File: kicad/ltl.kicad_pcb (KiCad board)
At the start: 2 copper layers, 98.6 x 63.2 mm, 66 parts, among them J1 J1, Q1 RUM001L02T2CL, Q2 RZM001P02T2L, Q3 BC327, U1 TPL5111, U2 ESP-12E, U3 DS18B20, U4 TPS73733DCQR

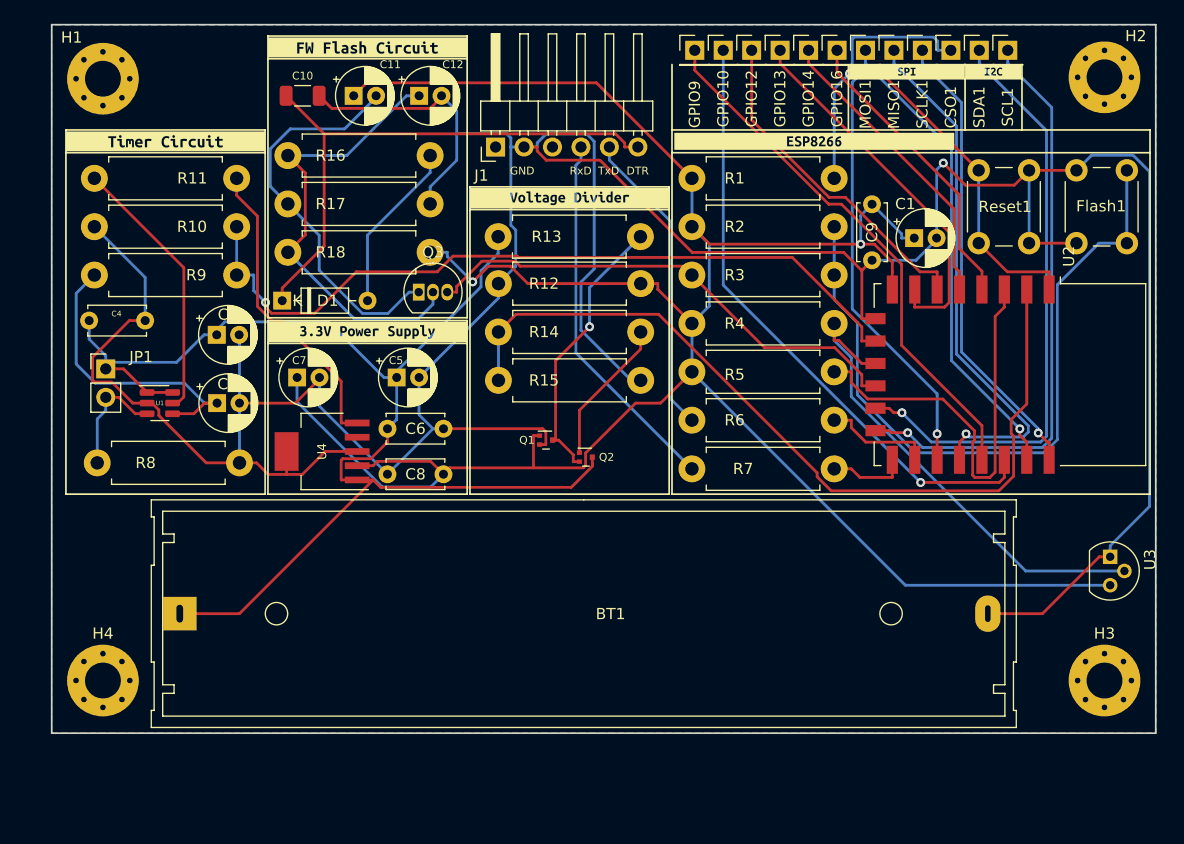
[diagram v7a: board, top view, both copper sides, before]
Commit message: Updated PCB to Revision 2.2
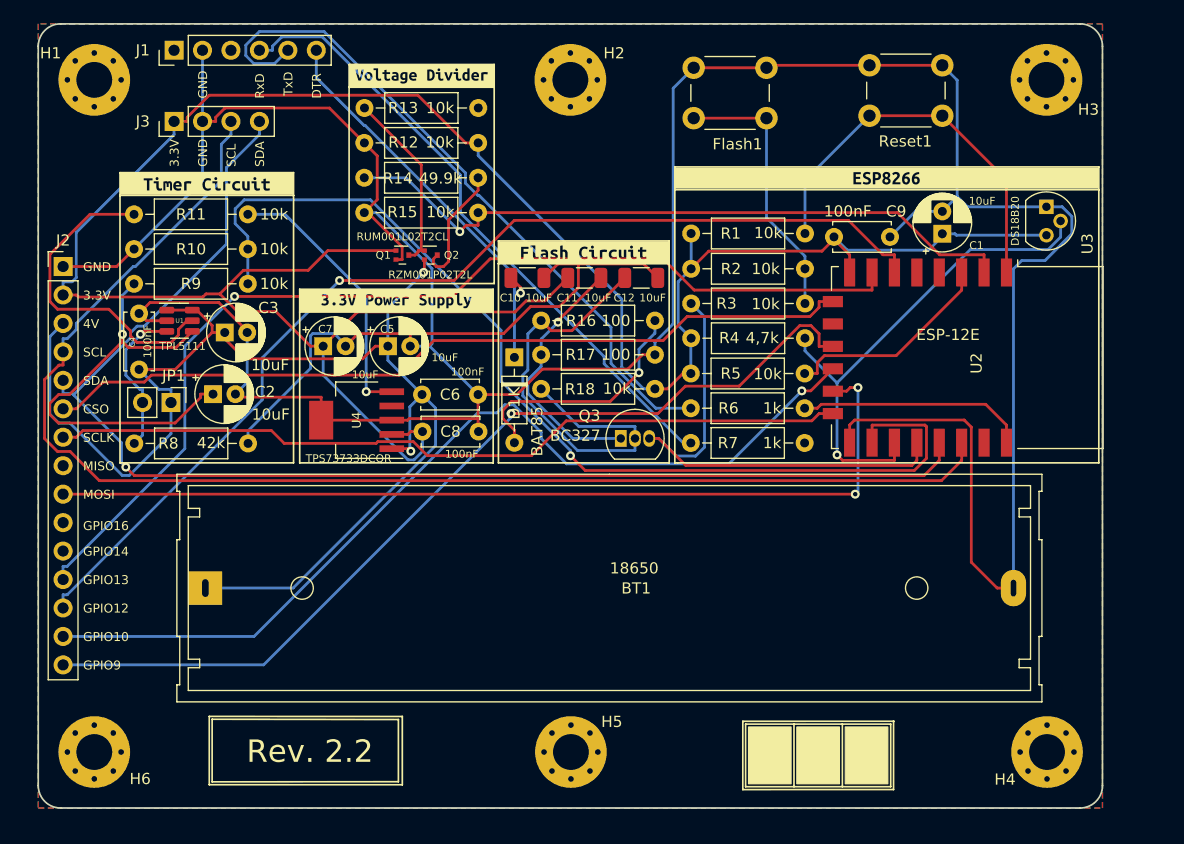
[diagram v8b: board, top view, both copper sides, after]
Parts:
- removed CSO1: CSO, Connector_PinHeader_2.54mm:PinHeader_1x01_P2.54mm_Vertical
- removed GPIO10: GPIO10, Connector_PinHeader_2.54mm:PinHeader_1x01_P2.54mm_Vertical
- removed GPIO12: GPIO12, Connector_PinHeader_2.54mm:PinHeader_1x01_P2.54mm_Vertical
- removed GPIO13: GPIO13, Connector_PinHeader_2.54mm:PinHeader_1x01_P2.54mm_Vertical
- removed GPIO14: GPIO14, Connector_PinHeader_2.54mm:PinHeader_1x01_P2.54mm_Vertical
- removed GPIO16: GPIO16, Connector_PinHeader_2.54mm:PinHeader_1x01_P2.54mm_Vertical
- removed GPIO9: GPIO9, Connector_PinHeader_2.54mm:PinHeader_1x01_P2.54mm_Vertical
- removed MISO1: MISO, Connector_PinHeader_2.54mm:PinHeader_1x01_P2.54mm_Vertical
- removed MOSI1: MOSI, Connector_PinHeader_2.54mm:PinHeader_1x01_P2.54mm_Vertical
- removed SCL1: SCL, Connector_PinHeader_2.54mm:PinHeader_1x01_P2.54mm_Vertical
- removed SCLK1: SCLK, Connector_PinHeader_2.54mm:PinHeader_1x01_P2.54mm_Vertical
- removed SDA1: SDA, Connector_PinHeader_2.54mm:PinHeader_1x01_P2.54mm_Vertical
- removed kibuzzard-65989638: G***, kibuzzard-65989638
- removed kibuzzard-65989978: G***, kibuzzard-65989978
- removed kibuzzard-65989B2E: G***, kibuzzard-65989B2E
- removed kibuzzard-65989B49: G***, kibuzzard-65989B49
- removed kibuzzard-65989BDF: G***, kibuzzard-65989BDF
- removed kibuzzard-65991234: G***, kibuzzard-65991234
- removed kibuzzard-659AB4FF: G***, kibuzzard-659AB4FF
- added H5: MountingHole, MountingHole:MountingHole_3.2mm_M3_Pad_Via, F.Cu at (122.5, 133.0)
- added H6: MountingHole, MountingHole:MountingHole_3.2mm_M3_Pad_Via, F.Cu at (80.0, 133.0)
- added J2: Conn_01x15, Connector_PinHeader_2.54mm:PinHeader_1x15_P2.54mm_Vertical, F.Cu at (77.2, 89.7)
- added J3: Conn_01x04, Connector_PinHeader_2.54mm:PinHeader_1x04_P2.54mm_Vertical, F.Cu at (87.1, 76.7)
- added kibuzzard-65AD8212: G***, kibuzzard-65AD8212, F.Cu at (90.0, 82.3)
- added kibuzzard-65AD85A3: G***, kibuzzard-65AD85A3, F.Cu at (123.7, 88.4)
- added kibuzzard-65AD86B5: G***, kibuzzard-65AD86B5, F.Cu at (107.0, 92.7)
- added kibuzzard-65AD8853: G***, kibuzzard-65AD8853, F.Cu at (109.2, 72.6)
- added kibuzzard-65AD8C40: G***, kibuzzard-65AD8C40, F.Cu at (150.7, 81.8)
- C11, C12: footprint Capacitor_THT:CP_Radial_D5.0mm_P2.00mm -> Capacitor_SMD:C_1206_3216Metric
- J1: value J1 -> Conn_01x06; footprint Connector_PinHeader_2.54mm:PinHeader_1x06_P2.54mm_Horizontal -> Connector_PinHeader_2.54mm:PinHeader_1x06_P2.54mm_Vertical
- R1, R10, R11, R12, R13, R14, R15, R16, R17, R18, R2, R3, R4, R5, R6, R7, R8, R9: footprint Resistor_THT:R_Axial_DIN0411_L9.9mm_D3.6mm_P12.70mm_Horizontal -> Resistor_THT:R_Axial_DIN0207_L6.3mm_D2.5mm_P10.16mm_Horizontal
- U2: footprint RF_Module:ESP-12E -> ESP8266MOD:ESP8266MOD
- moved H4 84.5 mm to (165.1, 133.0)
- moved H3 53.9 mm to (165.0, 73.0)
- moved H2 47.7 mm to (122.5, 73.0)
- moved Flash1 32.5 mm to (140.0, 76.4), turned to 180 degrees
- moved U3 31.8 mm to (165.0, 84.3)
- moved J1 30.0 mm to (87.1, 70.4)
- moved R15 28.9 mm to (104.1, 84.9), turned to 0 degrees
- moved R13 27.2 mm to (104.1, 75.5), turned to 0 degrees
- moved R16 27.0 mm to (119.9, 94.5)
- moved R17 26.3 mm to (119.9, 97.5)
- moved C11 26.2 mm to (123.7, 90.7)
- moved C10 25.8 mm to (118.7, 90.7)
- moved R18 25.7 mm to (119.9, 100.6)
- moved C12 25.6 mm to (128.8, 90.7)
- moved Q2 22.7 mm to (110.0, 88.6)
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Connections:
- Q2 pad 1: Net-(Q2-D) -> Net-(Q1-D)
- Q2 pad 2: Net-(Q1-D) -> +4V
- Q2 pad 3: +4V -> Net-(Q2-S)
- R14 pad 2: Net-(Q2-D) -> Net-(Q2-S)
- U2 pad 13: Net-(SDA1-Pin_1) -> SDA
- U2 pad 14: Net-(SCL1-Pin_1) -> SCL
- U2 pad 4: Net-(GPIO16-Pin_1) -> GPIO16
- U2 pad 5: Net-(GPIO14-Pin_1) -> GPIO14
- U2 pad 6: Net-(GPIO12-Pin_1) -> GPIO12
- U2 pad 7: Net-(GPIO13-Pin_1) -> GPIO13
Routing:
- net SCL: track 0.00 -> 121.5 mm
- net SDA: track 0.00 -> 117.3 mm, vias 0 -> 1
- net GPIO12: track 0.00 -> 94.3 mm, vias 0 -> 1
- net GPIO13: track 0.00 -> 92.9 mm, vias 0 -> 1
- net Net-(SDA1-Pin_1): track 53.7 -> 0.00 mm, vias 1 -> 0
- net Net-(SCL1-Pin_1): track 52.9 -> 0.00 mm, vias 1 -> 0
- net Net-(J2-Pin_8): track 47.5 -> 0.00 mm, vias 1 -> 0
- net Net-(J2-Pin_9): track 42.5 -> 82.7 mm, vias 1 -> 2
- net Net-(Flash1-Pad1): track 64.4 -> 24.5 mm
- net Net-(J2-Pin_15): track 47.8 -> 82.9 mm, vias 0 -> 1
- net /TxD: track 27.4 -> 62.1 mm
- net Net-(GPIO13-Pin_1): track 33.6 -> 0.00 mm
- net Net-(J2-Pin_7): track 41.3 -> 71.6 mm, vias 1 -> 0
- net Net-(GPIO12-Pin_1): track 30.0 -> 0.00 mm
- net Net-(J2-Pin_14): track 55.1 -> 83.3 mm
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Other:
- board size 98.6 x 63.2 mm -> 95 x 70 mm
- rule pad_to_mask_clearance: 0.2 -> 0
- board text added: "3.3V"
- board text added: "4V"
- board text added: "CSO"
- board text added: "GPIO10"
- board text added: "GPIO12"
- board text added: "GPIO13"
- board text added: "GPIO14"
- board text added: "GPIO16"
- board text added: "GPIO9"
- board text added: "MISO"
- board text added: "MOSI"
- board text added: "Rev. 2.2"
- board text added: "SCL"
- board text added: "SCLK"
- board text added: "SDA"
- board text removed: "Rev.2.0 Lfd.Nr."
